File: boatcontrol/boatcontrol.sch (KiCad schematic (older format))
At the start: 75 parts, among them J101 Conn_01x01_Male, J102 Conn_01x01_Male, J103 Conn_01x01_Male, J104 Raspberry_Pi_2_3, J105 Conn_01x02_Male, J106 Conn_01x01_Male, J107 SS73100-047F, J108 SS73100-047F, J109 Conn_01x01_Male, J110 Conn_01x01_Male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

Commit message: Fix graphics
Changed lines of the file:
@@
 Wire Wire Line
 	1750 9250 1750 9850
+Text Label 1450 9750 1    50   ~ 0
+12V_RAW
+$Comp
+L Graphic:Logo_Open_Hardware_Large #LOGO101
+U 1 1 637B1178
+P 15550 10450
+F 0 "#LOGO101" H 15550 10950 50  0001 C CNN
+F 1 "Logo_Open_Hardware_Large" H 15550 10050 50  0001 C CNN
+F 2 "" H 15550 10966 50  0001 C CNN
+F 3 "~" H 15550 10450 50  0001 C CNN
+	1    15550 10450
+	1    0    0    -1
+$EndComp
 Wire Bus Line
 	8700 1550 10500 1550
@@
 Wire Bus Line
 	7150 800  7150 4350
-Text Label 1450 9750 1    50   ~ 0
-12V_RAW
 $EndSCHEMATC

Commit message: Make 12V PSU Optional
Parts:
- added JP?: 12V PSU Bypass, symbol Jumper:SolderJumper_2_Open
- J111: Type 12VDC Logic -> 12VDC (OR 15-30V with 12V PSU)
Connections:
- wire segments 478 -> 480
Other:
- note added: "DC-DC Switching PSU(s)"
- note added: "Optional 12V PSU\nAllows Input voltages from \n15-30V DC"
- note removed: "12V & 5V DC-DC Power Supplies"
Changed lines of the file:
@@
 P 5400 9700
 F 0 "D101" V 5250 9800 50  0000 C CNN
-F 1 "MBR745" V 5650 9700 50  0000 C CNN
+F 1 "MBR745" V 5400 9900 50  0000 C CNN
 F 2 "BoatControl:TO-220" H 5400 9700 50  0001 C CNN
 F 3 "~" H 5400 9700 50  0001 C CNN
@@
 P 5400 10800
 F 0 "D102" V 5250 10900 50  0000 C CNN
-F 1 "MBR745" V 5650 10800 50  0000 C CNN
+F 1 "MBR745" V 5400 11000 50  0000 C CNN
 F 2 "BoatControl:TO-220" H 5400 10800 50  0001 C CNN
 F 3 "~" H 5400 10800 50  0001 C CNN
@@
 Wire Wire Line
 	2550 9450 2550 9850
-$Comp
-L power:GND #PWR0122
-U 1 1 602AEA4D
-P 1600 10950
-F 0 "#PWR0122" H 1600 10700 50  0001 C CNN
-F 1 "GND" H 1605 10777 50  0000 C CNN
-F 2 "" H 1600 10950 50  0001 C CNN
-F 3 "" H 1600 10950 50  0001 C CNN
-	1    1600 10950
-	1    0    0    -1
-$EndComp
 Wire Wire Line
 	3100 10700 3100 10950
@@
 	1    0    0    -1
 $EndComp
-Wire Wire Line
-	2000 10950 2000 9850
-Connection ~ 2000 10950
 $Comp
 L BoatControl:TBL008V-1000-02BE J111
@@
 F 2 "CUI_TBL008V-1000-02BE" H 1000 9750 50  0001 L BNN
 F 3 "CUI" H 1000 9750 50  0001 L BNN
-F 4 "12VDC Logic" H 950 10000 50  0000 C CNN "Type"
+F 4 "12VDC (OR 15-30V with 12V PSU)" H 750 10000 50  0000 C CNN "Type"
 	1    1000 9750
 	-1   0    0    1
@@
 L power:+5V #PWR0120
 U 1 1 F43573A4
-P 6600 9300
-F 0 "#PWR0120" H 6600 9150 50  0001 C CNN
-F 1 "+5V" H 6615 9473 50  0000 C CNN
-F 2 "" H 6600 9300 50  0001 C CNN
-F 3 "" H 6600 9300 50  0001 C CNN
-	1    6600 9300
+P 7050 9300
+F 0 "#PWR0120" H 7050 9150 50  0001 C CNN
+F 1 "+5V" H 7065 9473 50  0000 C CNN
+F 2 "" H 7050 9300 50  0001 C CNN
+F 3 "" H 7050 9300 50  0001 C CNN
+	1    7050 9300
 	-1   0    0    1
 $EndComp
@@
 Wire Wire Line
 	5400 10950 6000 10950
-Wire Wire Line
-	1600 10950 2000 10950
 Wire Wire Line
 	1600 8850 1750 8850
 Connection ~ 1600 8850
-Wire Wire Line
-	1600 10950 1450 10950
-Wire Wire Line
-	1450 10950 1450 9850
-Wire Wire Line
-	1450 9850 1400 9850
-Connection ~ 1600 10950
 Wire Wire Line
 	1400 9750 1450 9750
@@
 	14300 1250 14300 1450
 Text Notes 5350 8650 0    50   ~ 0
-12V & 5V DC-DC Power Supplies
+DC-DC Switching PSU(s)
 Wire Notes Line
 	6800 8500 550  8500
@@
 L power:PWR_FLAG #FLG0104
 U 1 1 5F134FC1
-P 6600 9300
-F 0 "#FLG0104" H 6600 9375 50  0001 C CNN
-F 1 "PWR_FLAG" H 6600 9473 50  0000 C CNN
-F 2 "" H 6600 9300 50  0001 C CNN
-F 3 "~" H 6600 9300 50  0001 C CNN
-	1    6600 9300
+P 7050 9300
+F 0 "#FLG0104" H 7050 9375 50  0001 C CNN
+F 1 "PWR_FLAG" H 7050 9473 50  0000 C CNN
+F 2 "" H 7050 9300 50  0001 C CNN
+F 3 "~" H 7050 9300 50  0001 C CNN
+	1    7050 9300
 	1    0    0    -1
 $EndComp
@@
 L power:PWR_FLAG #FLG0106
 U 1 1 5F2FEC8F
-P 1450 10950
-F 0 "#FLG0106" H 1450 11025 50  0001 C CNN
-F 1 "PWR_FLAG" V 1450 11078 50  0000 L CNN
-F 2 "" H 1450 10950 50  0001 C CNN
-F 3 "~" H 1450 10950 50  0001 C CNN
-	1    1450 10950
-	0    -1   -1   0
-$EndComp
-Connection ~ 1450 10950
+P 1850 9850
+F 0 "#FLG0106" H 1850 9925 50  0001 C CNN
+F 1 "PWR_FLAG" H 1800 10000 50  0000 L CNN
+F 2 "" H 1850 9850 50  0001 C CNN
+F 3 "~" H 1850 9850 50  0001 C CNN
+	1    1850 9850
+	1    0    0    -1
+$EndComp
 $Comp
 L power:+5V #PWR0104
@@
 	1    0    0    -1
 $EndComp
-Connection ~ 6600 9300
+Connection ~ 7050 9300
 Wire Wire Line
 	1450 8850 1600 8850
@@
 	1    0    0    -1
 $EndComp
-Connection ~ 6600 10400
+Connection ~ 7050 10400
 $Comp
 L power:PWR_FLAG #FLG0105
 U 1 1 5F13965C
-P 6600 10400
-F 0 "#FLG0105" H 6600 10475 50  0001 C CNN
-F 1 "PWR_FLAG" H 6600 10573 50  0000 C CNN
-F 2 "" H 6600 10400 50  0001 C CNN
-F 3 "~" H 6600 10400 50  0001 C CNN
-	1    6600 10400
+P 7050 10400
+F 0 "#FLG0105" H 7050 10475 50  0001 C CNN
+F 1 "PWR_FLAG" H 7050 10573 50  0000 C CNN
+F 2 "" H 7050 10400 50  0001 C CNN
+F 3 "~" H 7050 10400 50  0001 C CNN
+	1    7050 10400
 	1    0    0    -1
 $EndComp
@@
 L power:+12P #PWR0121
 U 1 1 603A75D7
-P 6600 10400
-F 0 "#PWR0121" H 6600 10250 50  0001 C CNN
-F 1 "+12P" H 6615 10573 50  0000 C CNN
-F 2 "" H 6600 10400 50  0001 C CNN
-F 3 "" H 6600 10400 50  0001 C CNN
-	1    6600 10400
+P 7050 10400
+F 0 "#PWR0121" H 7050 10250 50  0001 C CNN
+F 1 "+12P" H 7065 10573 50  0000 C CNN
+F 2 "" H 7050 10400 50  0001 C CNN
+F 3 "" H 7050 10400 50  0001 C CNN
+	1    7050 10400
 	-1   0    0    1
 $EndComp
@@
 Wire Wire Line
 	6300 9450 6300 9300
-Connection ~ 6300 9300
-Wire Wire Line
-	6300 9300 6600 9300
 Connection ~ 6150 9300
 Wire Wire Line
@@
 	6300 10550 6300 10400
 Connection ~ 6300 10400
-Wire Wire Line
-	6300 10400 6600 10400
 Connection ~ 2550 8850
 Wire Wire Line
@@
 Wire Wire Line
 	2250 8850 2550 8850
-Wire Wire Line
-	2000 9850 2550 9850
 Connection ~ 2550 9950
 Wire Wire Line
@@
 Wire Wire Line
 	2550 10950 2700 10950
-Wire Wire Line
-	2000 10950 2550 10950
 Wire Wire Line
 	2250 9950 2550 9950
@@
 Wire Wire Line
 	1450 8850 1450 9050
-Wire Wire Line
-	1450 9850 1750 9850
-Connection ~ 1450 9850
 $Comp
 L power:+12P #PWR0116
@@
 Wire Notes Line
 	2550 8700 2550 8550
-Wire Notes Line
-	3200 10000 6750 10000
 Wire Wire Line
 	1750 9250 1750 9850
@@
 	1    0    0    -1
 $EndComp
+Text Notes 600  10350 0    50   ~ 0
+Optional 12V PSU\nAllows Input voltages from \n15-30V DC
+$Comp
+L Jumper:SolderJumper_2_Open JP?
+U 1 1 6052E1CB
+P 6600 10250
+F 0 "JP?" V 6850 10200 50  0000 L CNN
+F 1 "12V PSU Bypass" V 6450 9600 50  0000 L CNN
+F 2 "" H 6600 10250 50  0001 C CNN
+F 3 "~" H 6600 10250 50  0001 C CNN
+	1    6600 10250
+	0    1    1    0
+$EndComp
+Connection ~ 6300 9300
+Wire Wire Line
+	6300 9300 7050 9300
+Connection ~ 6600 10400
+Wire Wire Line
+	6600 10400 7050 10400
+Wire Wire Line
+	3100 9950 6600 9950
+Wire Wire Line
+	6600 9950 6600 10100
+Wire Wire Line
+	6300 10400 6600 10400
+Connection ~ 3100 9950
+Wire Notes Line
+	550  10050 6800 10050
+Connection ~ 1750 9850
+Wire Wire Line
+	1400 9850 1750 9850
+Wire Wire Line
+	1750 9850 1850 9850
+Wire Wire Line
+	2200 9850 2200 10950
 Wire Bus Line
 	8700 1550 10500 1550
@@
 Wire Bus Line
 	7150 800  7150 4350
+Connection ~ 2200 9850
+Wire Wire Line
+	2200 9850 2550 9850
+Wire Wire Line
+	2200 10950 2550 10950
+Connection ~ 2050 9850
+Wire Wire Line
+	2050 9850 2200 9850
+Connection ~ 1850 9850
+Wire Wire Line
+	1850 9850 2050 9850
+$Comp
+L power:GND #PWR0122
+U 1 1 602AEA4D
+P 2050 9850
+F 0 "#PWR0122" H 2050 9600 50  0001 C CNN
+F 1 "GND" H 2050 9700 50  0000 C CNN
+F 2 "" H 2050 9850 50  0001 C CNN
+F 3 "" H 2050 9850 50  0001 C CNN
+	1    2050 9850
+	1    0    0    -1
+$EndComp
 $EndSCHEMATC

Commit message: Logo stuff
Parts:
- JP110: renamed from JP?; footprint (none) -> Jumper:SolderJumper-2_P1.3mm_Open_RoundedPad1.0x1.5mm
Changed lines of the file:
@@
 12V_RAW
 $Comp
-L Graphic:Logo_Open_Hardware_Large #LOGO101
+L Graphic:Logo_Open_Hardware_Small #LOGO101
 U 1 1 637B1178
-P 15550 10450
-F 0 "#LOGO101" H 15550 10950 50  0001 C CNN
-F 1 "Logo_Open_Hardware_Large" H 15550 10050 50  0001 C CNN
-F 2 "" H 15550 10966 50  0001 C CNN
-F 3 "~" H 15550 10450 50  0001 C CNN
-	1    15550 10450
+P 15800 10300
+F 0 "#LOGO101" H 15800 10800 50  0001 C CNN
+F 1 "Open Hardware" H 15800 9900 50  0001 C CNN
+F 2 "Symbol:OSHW-Logo2_48.7x40mm_SilkScreen" H 15800 10816 50  0001 C CNN
+F 3 "~" H 15800 10300 50  0001 C CNN
+	1    15800 10300
 	1    0    0    -1
 $EndComp
@@
 Optional 12V PSU\nAllows Input voltages from \n15-30V DC
 $Comp
-L Jumper:SolderJumper_2_Open JP?
+L Jumper:SolderJumper_2_Open JP110
 U 1 1 6052E1CB
 P 6600 10250
-F 0 "JP?" V 6850 10200 50  0000 L CNN
+F 0 "JP110" V 6850 10200 50  0000 L CNN
 F 1 "12V PSU Bypass" V 6450 9600 50  0000 L CNN
-F 2 "" H 6600 10250 50  0001 C CNN
+F 2 "Jumper:SolderJumper-2_P1.3mm_Open_RoundedPad1.0x1.5mm" H 6600 10250 50  0001 C CNN
 F 3 "~" H 6600 10250 50  0001 C CNN
 	1    6600 10250
@@
 Wire Wire Line
 	2200 9850 2200 10950
-Wire Bus Line
-	8700 1550 10500 1550
-Wire Bus Line
-	8700 1550 8700 4350
-Wire Bus Line
-	10500 1550 10500 4350
-Wire Bus Line
-	7150 800  7150 4350
 Connection ~ 2200 9850
 Wire Wire Line
@@
 	1    0    0    -1
 $EndComp
+Wire Bus Line
+	8700 1550 10500 1550
+Wire Bus Line
+	8700 1550 8700 4350
+Wire Bus Line
+	10500 1550 10500 4350
+Wire Bus Line
+	7150 800  7150 4350
 $EndSCHEMATC

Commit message: Add art and logos
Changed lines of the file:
@@
+	1    0    0    -1
+$EndComp
+$Comp
+L BoatControl:LOGO_RUGLUDALLUR #G?
+U 1 1 5FEB07B2
+P 15650 9500
+F 0 "#G?" H 15650 9190 60  0001 C CNN
+F 1 "LOGO_RUGLUDALLUR" H 15650 9810 60  0001 C CNN
+F 2 "BoatControl:Rugludallur-Logo_SilkScreen" H 15649 9907 50  0001 C CNN
+F 3 "" H 15650 9500 50  0001 C CNN
+	1    15650 9500
+	1    0    0    -1
+$EndComp
+$Comp
+L BoatControl:LOGO_ANT #G?
+U 1 1 5FEB4243
+P 14800 9500
+F 0 "#G?" H 14800 9170 60  0001 C CNN
+F 1 "LOGO_ANT" H 14800 9830 60  0001 C CNN
+F 2 "BoatControl:Ant_Logo_SilkScreen" H 14797 9923 50  0001 C CNN
+F 3 "" H 14800 9500 50  0001 C CNN
+	1    14800 9500
 	1    0    0    -1
 $EndComp
@@
 Wire Bus Line
 	7150 800  7150 4350
+$Comp
+L Graphic:Logo_Open_Hardware_Small #LOGO?
+U 1 1 60207FB9
+P 15200 10300
+F 0 "#LOGO?" H 15200 10575 50  0001 C CNN
+F 1 "Logo_Open_Hardware_Small" H 15200 10075 50  0001 C CNN
+F 2 "Symbol:KiCad-Logo_40mm_SilkScreen" H 15200 10300 50  0001 C CNN
+F 3 "~" H 15200 10300 50  0001 C CNN
+	1    15200 10300
+	1    0    0    -1
+$EndComp
 $EndSCHEMATC

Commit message: Relays and Fuses in place
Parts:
- added G101: LOGO_ANT, BoatControl:Ant_Logo_SilkScreen, symbol BoatControl:LOGO_ANT
- added G102: LOGO_RUGLUDALLUR, BoatControl:Rugludallur-Logo_SilkScreen, symbol BoatControl:LOGO_RUGLUDALLUR
- added LOGO101: Open Hardware, Symbol:OSHW-Logo2_48.7x40mm_SilkScreen, symbol Graphic:Logo_Open_Hardware_Small
- added LOGO102: Logo_Open_Hardware_Small, Symbol:KiCad-Logo2_40mm_SilkScreen, symbol Graphic:Logo_Open_Hardware_Small
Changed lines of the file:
@@
 12V_RAW
 $Comp
-L Graphic:Logo_Open_Hardware_Small #LOGO101
+L Graphic:Logo_Open_Hardware_Small LOGO101
 U 1 1 637B1178
 P 15800 10300
-F 0 "#LOGO101" H 15800 10800 50  0001 C CNN
+F 0 "LOGO101" H 15800 10800 50  0001 C CNN
 F 1 "Open Hardware" H 15800 9900 50  0001 C CNN
 F 2 "Symbol:OSHW-Logo2_48.7x40mm_SilkScreen" H 15800 10816 50  0001 C CNN
@@
 $EndComp
 $Comp
-L BoatControl:LOGO_RUGLUDALLUR #G?
+L BoatControl:LOGO_RUGLUDALLUR G102
 U 1 1 5FEB07B2
 P 15650 9500
-F 0 "#G?" H 15650 9190 60  0001 C CNN
+F 0 "G102" H 15650 9190 60  0001 C CNN
 F 1 "LOGO_RUGLUDALLUR" H 15650 9810 60  0001 C CNN
 F 2 "BoatControl:Rugludallur-Logo_SilkScreen" H 15649 9907 50  0001 C CNN
@@
 $EndComp
 $Comp
-L BoatControl:LOGO_ANT #G?
+L BoatControl:LOGO_ANT G101
 U 1 1 5FEB4243
 P 14800 9500
-F 0 "#G?" H 14800 9170 60  0001 C CNN
+F 0 "G101" H 14800 9170 60  0001 C CNN
 F 1 "LOGO_ANT" H 14800 9830 60  0001 C CNN
 F 2 "BoatControl:Ant_Logo_SilkScreen" H 14797 9923 50  0001 C CNN
@@
 	7150 800  7150 4350
 $Comp
-L Graphic:Logo_Open_Hardware_Small #LOGO?
+L Graphic:Logo_Open_Hardware_Small LOGO102
 U 1 1 60207FB9
 P 15200 10300
-F 0 "#LOGO?" H 15200 10575 50  0001 C CNN
+F 0 "LOGO102" H 15200 10575 50  0001 C CNN
 F 1 "Logo_Open_Hardware_Small" H 15200 10075 50  0001 C CNN
-F 2 "Symbol:KiCad-Logo_40mm_SilkScreen" H 15200 10300 50  0001 C CNN
+F 2 "Symbol:KiCad-Logo2_40mm_SilkScreen" H 15200 10300 50  0001 C CNN
 F 3 "~" H 15200 10300 50  0001 C CNN
 	1    15200 10300

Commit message: Bottom done
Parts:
- removed Q102: IRF9510PBF-BE3, Package_TO_SOT_THT:TO-220-3_Vertical, symbol BoatControl:IPP_B_I80P03
- added Q102: IPP120P04P4L-03, Package_TO_SOT_THT:TO-220-3_Vertical, symbol BoatControl:IPP120P04P4L-03
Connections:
- net +12V: now also Q102.3 (S)
- net 12V_RAW: now also Q102.2 (D)
- net GND: now also Q102.1 (G)
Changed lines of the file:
@@
 Text GLabel 15000 3650 2    50   Input ~ 0
 12V_DC_C23_ON
-$Comp
-L BoatControl:IPP_B_I80P03 Q102
-U 1 1 63241E20
-P 1450 9250
-AR Path="/63241E20" Ref="Q102"  Part="1"
-AR Path="/D16552B4/63241E20" Ref="Q?"  Part="1"
-F 0 "Q102" V 1300 9050 50  0000 L CNN
-F 1 "IRF9510PBF-BE3" V 1600 8950 50  0000 L CNN
-F 2 "Package_TO_SOT_THT:TO-220-3_Vertical" H 1450 9250 50  0001 C CNN
-F 3 "https://www.vishay.com/docs/91072/91072.pdf" H 1450 9250 50  0001 C CNN
-F 4 "P-Channel 100V 4A (Tc) 43W (Tc) Through Hole TO-220AB" H 1450 9250 50  0001 C CNN "Description"
-F 5 "Vishay Siliconix" H 1450 9250 50  0001 C CNN "Manufacturer"
-	1    1450 9250
-	-1   0    0    1
-$EndComp
 Text Notes 600  8600 0    50   ~ 0
 Reverse polarity and over-current protection
@@
 	1    0    0    -1
 $EndComp
-Wire Bus Line
-	8700 1550 10500 1550
-Wire Bus Line
-	8700 1550 8700 4350
-Wire Bus Line
-	10500 1550 10500 4350
-Wire Bus Line
-	7150 800  7150 4350
 $Comp
 L Graphic:Logo_Open_Hardware_Small LOGO102
@@
 	1    0    0    -1
 $EndComp
+Wire Bus Line
+	8700 1550 10500 1550
+Wire Bus Line
+	8700 1550 8700 4350
+Wire Bus Line
+	10500 1550 10500 4350
+Wire Bus Line
+	7150 800  7150 4350
+$Comp
+L BoatControl:IPP120P04P4L-03 Q102
+U 1 1 5FE81B4F
+P 1450 9250
+F 0 "Q102" H 1555 9204 50  0000 L CNN
+F 1 "IPP120P04P4L-03" H 1555 9295 50  0000 L CNN
+F 2 "Package_TO_SOT_THT:TO-220-3_Vertical" H 1100 9800 50  0001 C CNN
+F 3 "https://www.infineon.com/dgdl/Infineon-I80P03P4L_04-DS-v01_01-en.pdf?folderId=db3a304314dca3890114ef902baa05f9&fileId=db3a30431ddc9372011e07e95eb827d7&ack=t" H 1450 9250 50  0001 C CNN
+F 4 "P-Channel 30V 80A (Tc) 137W (Tc) Through Hole PG-TO220-3-1" H 1300 9900 50  0001 C CNN "Description"
+F 5 "OptiMOS" H 2050 9550 50  0001 C CNN "Series"
+F 6 "Infineon Technologies" H 1950 9650 50  0001 C CNN "Infineon Technologies"
+	1    1450 9250
+	-1   0    0    1
+$EndComp
 $EndSCHEMATC

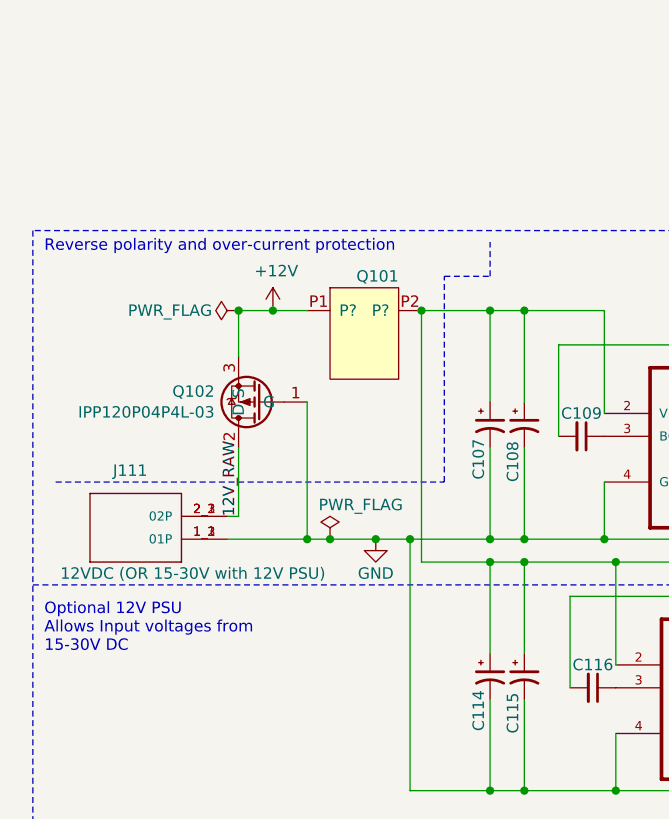
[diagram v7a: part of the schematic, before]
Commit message: Add reverse/AC/DC polarity indicators
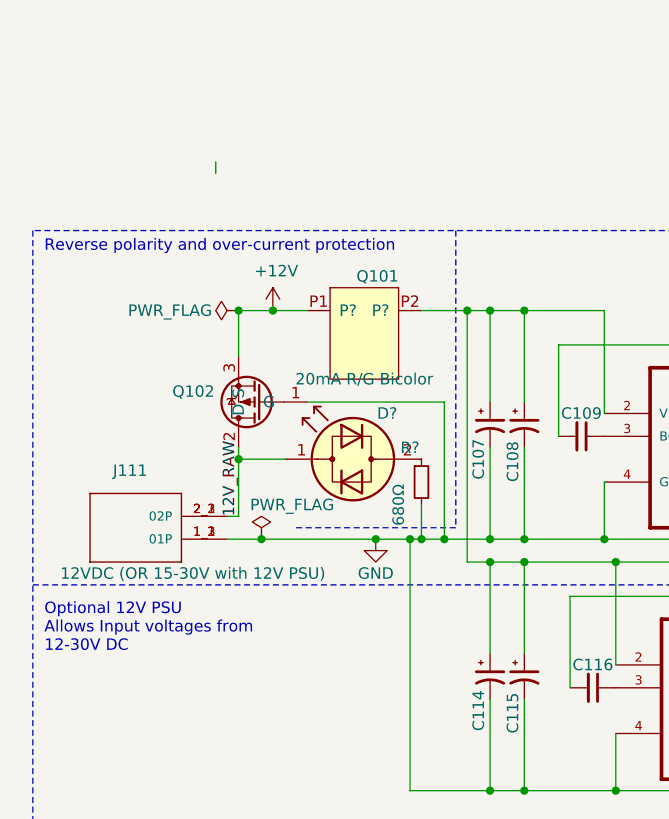
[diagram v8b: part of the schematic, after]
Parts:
- added D?: 20mA R/G Bicolor, LED_THT:LED_D5.0mm, symbol Device:LED_Dual_2pin
- added R?: 680Ω, Resistor_THT:R_Axial_DIN0207_L6.3mm_D2.5mm_P7.62mm_Horizontal, symbol Device:R_Small
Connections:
- net 12V_RAW: now also D?.1 (KA)
- net GND: now also R?.2
- new net: D?.2 (AK), R?.1
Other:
- note added: "Optional 12V PSU\nAllows Input voltages from \n12-30V DC"
- note removed: "Optional 12V PSU\nAllows Input voltages from \n15-30V DC"
